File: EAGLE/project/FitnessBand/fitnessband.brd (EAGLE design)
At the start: 40 x 30.1 mm, 57 parts, among them J5 TC2030-JLINK-NL, U17 NRF51822QF, X3 EPSON-FA-128, X4 ABS05-32.768KHZ-T, X5 USB-MICROB

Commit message: ready to order
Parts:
- moved C13_IMU 8.82 mm to (35.3, 26.2)
- moved R9_IMU 8.21 mm to (26.4, 26.5), flipped to the top, turned to 270 degrees
- moved C7_IMU 6.41 mm to (27.5, 22.6), flipped to the top, turned to 180 degrees
- moved C8_IMU 5.74 mm to (33.8, 27.0), turned to 270 degrees
- moved R3_LED 5.30 mm to (6.24, 26.6), turned to 0 degrees
- moved C12_IMU 2.98 mm to (32.4, 22.8), turned to 180 degrees
- moved R5_IMU 1.71 mm to (31.7, 27.1)
- moved IMU 0.58 mm to (30.2, 26.0), flipped to the top
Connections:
- net SCL_IMU: now also U17.44; no longer U17.43
- net SDA_IMU: now also U17.43; no longer U17.44
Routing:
- net SDA_IMU: track 18.4 -> 31.7 mm, vias 1 -> 0
- net SCL_IMU: track 23.1 -> 29.3 mm
- net N$49: track 6.55 -> 2.75 mm, vias 0 -> 1
- net N$48: track 1.45 -> 4.72 mm, vias 0 -> 1
- net INT_IMU: track 10.8 -> 13.9 mm, vias 1 -> 2
- net GND: track 40.6 -> 37.5 mm, vias 38 -> 36
- net SCLK_LCD: track 19.4 -> 16.6 mm
- net SCS_LCD: track 15.1 -> 12.5 mm
- net SI_LCD: track 17.3 -> 14.8 mm
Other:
- board text added: "The EIR REV1 The Watchmen EECS 473 F15"

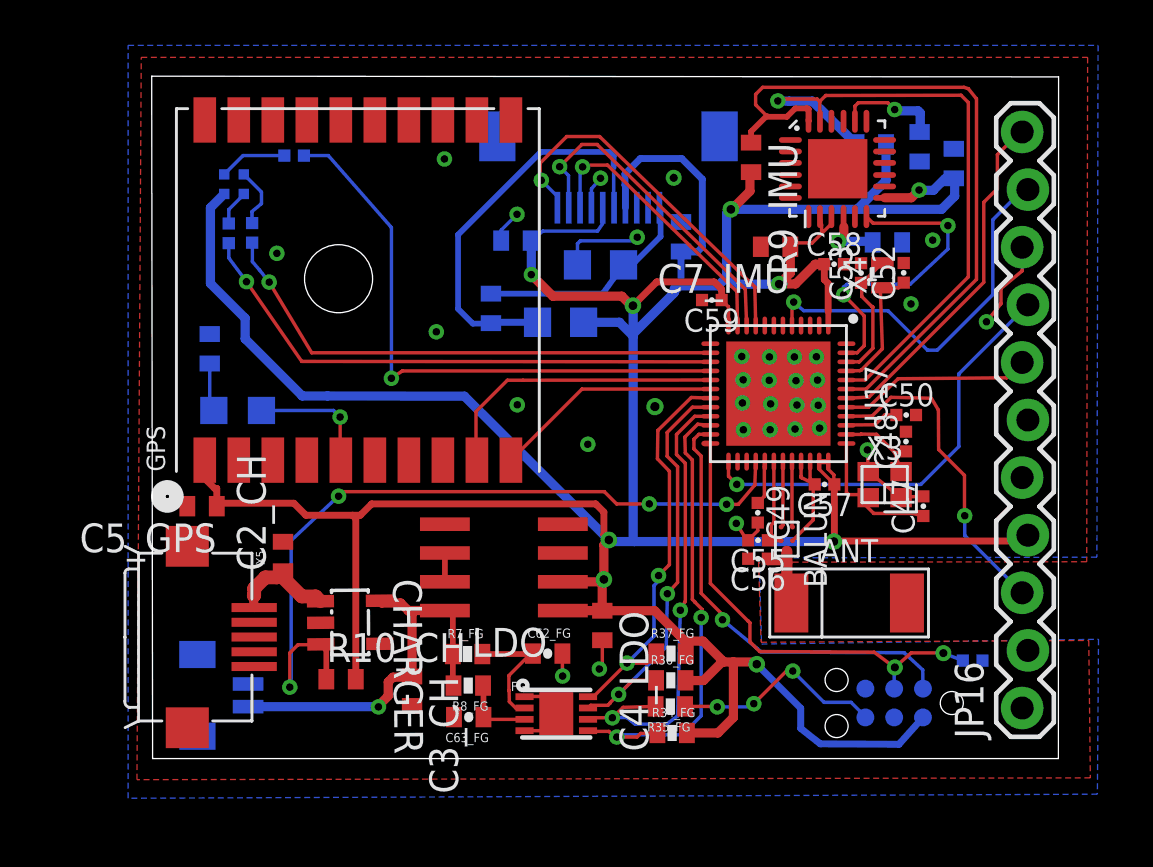
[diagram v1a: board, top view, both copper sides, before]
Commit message: rearranged imu
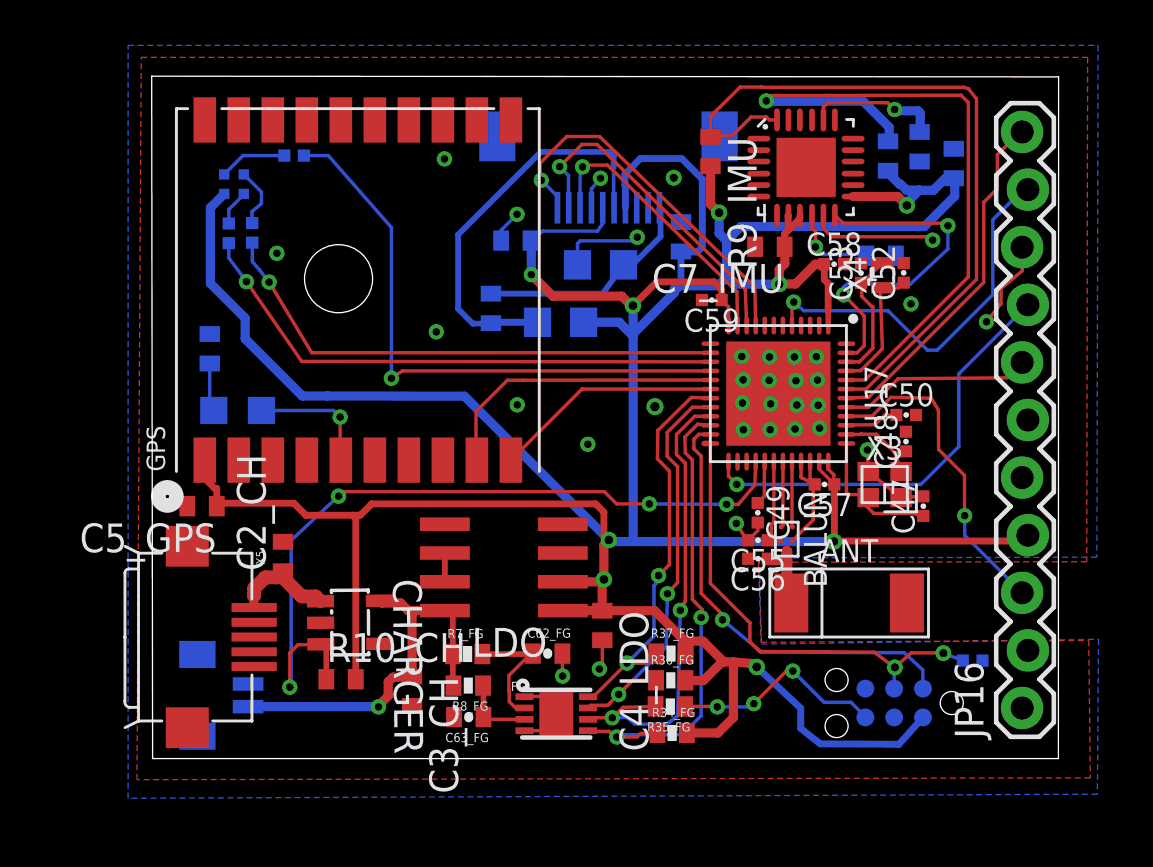
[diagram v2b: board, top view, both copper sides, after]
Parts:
- moved R9_IMU 1.81 mm to (24.6, 26.8)
- moved IMU 1.39 mm to (28.8, 26.1)
- moved R5_IMU 0.90 mm to (32.4, 26.6), turned to 270 degrees
- moved C12_IMU 0.65 mm to (32.1, 22.2)
- moved C7_IMU 0.25 mm to (27.2, 22.6)
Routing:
- net GND: track 37.5 -> 43.1 mm
- net SCL_IMU: track 29.3 -> 31.0 mm
- net INT_IMU: track 13.9 -> 15.3 mm
- net N$48: track 4.72 -> 5.96 mm
- net N$49: track 2.75 -> 3.86 mm
- net SDA_IMU: track 31.7 -> 32.4 mm
